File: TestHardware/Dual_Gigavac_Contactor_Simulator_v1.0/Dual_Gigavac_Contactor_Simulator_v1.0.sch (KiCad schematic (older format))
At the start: 69 parts, among them J1 Signal, J2 Power, J3 Contactor Driver 1, J4 Contactor Sense 2, J5 Contactor Sense 1, J6 Contactor Driver 2, Q1 Q_NMOS_DUAL_SGD, Q2 Q_NMOS_DUAL_SGD, Q3 Q_NMOS_DUAL_SGD, SW1 SW_Push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

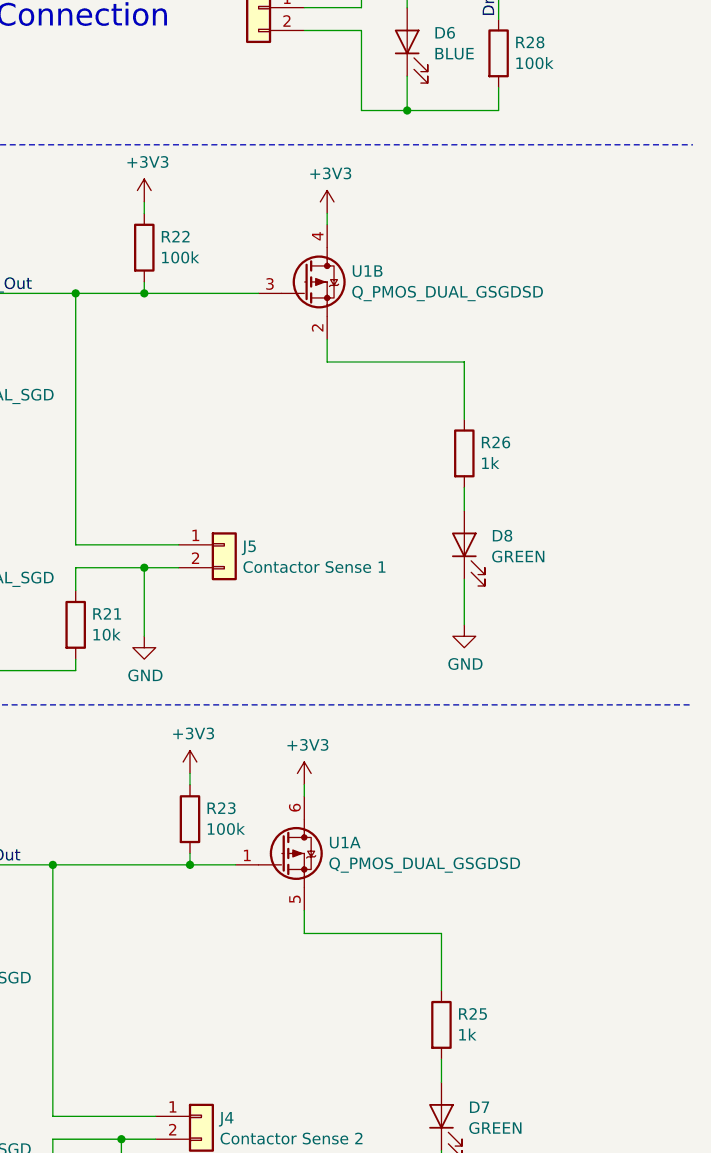
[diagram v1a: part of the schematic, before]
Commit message: Fix U1A & B Orientation
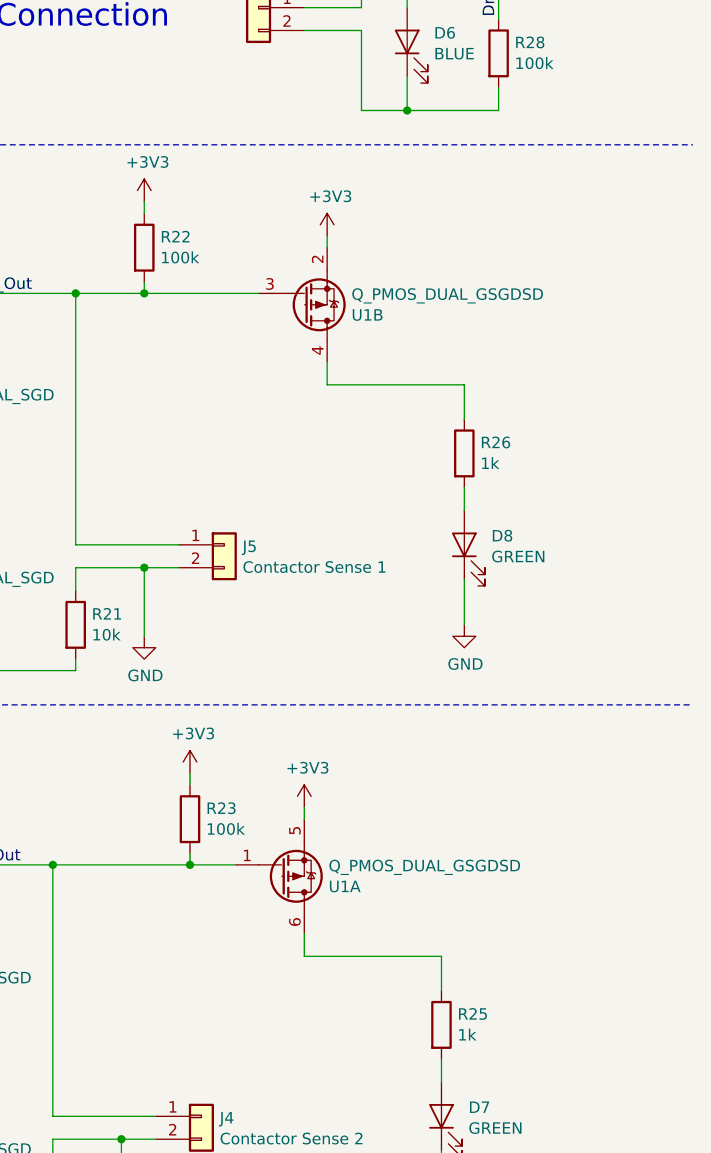
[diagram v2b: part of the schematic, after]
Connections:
- net +3V3: now also U1.2 (Source), U1.5 (Source); no longer U1.4 (Drain), U1.6 (Drain)
- net at R26.1: now also U1.4 (Drain); no longer U1.2 (Source)
- net at R25.1: now also U1.6 (Drain); no longer U1.5 (Source)
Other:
- moved on the sheet: U1A, U1B
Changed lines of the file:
@@
 EESchema Schematic File Version 4
+LIBS:Dual_Gigavac_Contactor_Simulator_v1.0-cache
 EELAYER 26 0
 EELAYER END
@@
 L Discrete_SMD:Q_PMOS_DUAL_GSGDSD U1
 U 2 1 5F0C1AAE
-P 8750 2450
-F 0 "U1" H 8906 2496 50  0000 L CNN
-F 1 "Q_PMOS_DUAL_GSGDSD" H 8906 2405 50  0000 L CNN
-F 2 "Package_TO_SOT_SMD:SuperSOT-6" H 8900 2550 50  0001 C CNN
-F 3 "https://www.onsemi.com/pub/Collateral/NDC7003P-D.PDF" H 8700 2450 50  0001 C CNN
-F 4 "NDC7003P " H 0   0   50  0001 C CNN "MPN"
-	2    8750 2450
-	1    0    0    -1
+P 8750 2550
+F 0 "U1" H 8906 2596 50  0000 L CNN
+F 1 "Q_PMOS_DUAL_GSGDSD" H 8906 2505 50  0000 L CNN
+F 2 "Package_TO_SOT_SMD:SuperSOT-6" H 8900 2650 50  0001 C CNN
+F 3 "https://www.onsemi.com/pub/Collateral/NDC7003P-D.PDF" H 8700 2550 50  0001 C CNN
+F 4 "NDC7003P " H 0   100 50  0001 C CNN "MPN"
+	2    8750 2550
+	1    0    0    1
 $EndComp
 $Comp
 L Discrete_SMD:Q_PMOS_DUAL_GSGDSD U1
 U 1 1 5F0C1B3D
-P 8650 4950
-F 0 "U1" H 8806 4996 50  0000 L CNN
-F 1 "Q_PMOS_DUAL_GSGDSD" H 8806 4905 50  0000 L CNN
-F 2 "Package_TO_SOT_SMD:SuperSOT-6" H 8800 5050 50  0001 C CNN
-F 3 "https://www.onsemi.com/pub/Collateral/NDC7003P-D.PDF" H 8600 4950 50  0001 C CNN
-F 4 "NDC7003P " H 0   0   50  0001 C CNN "MPN"
-	1    8650 4950
-	1    0    0    -1
+P 8650 5050
+F 0 "U1" H 8806 5096 50  0000 L CNN
+F 1 "Q_PMOS_DUAL_GSGDSD" H 8806 5005 50  0000 L CNN
+F 2 "Package_TO_SOT_SMD:SuperSOT-6" H 8800 5150 50  0001 C CNN
+F 3 "https://www.onsemi.com/pub/Collateral/NDC7003P-D.PDF" H 8600 5050 50  0001 C CNN
+F 4 "NDC7003P " H 0   100 50  0001 C CNN "MPN"
+	1    8650 5050
+	1    0    0    1
 $EndComp
 Wire Wire Line
@@
 L power:+3V3 #PWR011
 U 1 1 5F124D0E
-P 8800 2150
-F 0 "#PWR011" H 8800 2000 50  0001 C CNN
-F 1 "+3V3" H 8815 2323 50  0000 C CNN
-F 2 "" H 8800 2150 50  0001 C CNN
-F 3 "" H 8800 2150 50  0001 C CNN
-	1    8800 2150
-	1    0    0    -1
-$EndComp
-Wire Wire Line
-	8800 2200 8800 2150
+P 8800 2250
+F 0 "#PWR011" H 8800 2100 50  0001 C CNN
+F 1 "+3V3" H 8815 2423 50  0000 C CNN
+F 2 "" H 8800 2250 50  0001 C CNN
+F 3 "" H 8800 2250 50  0001 C CNN
+	1    8800 2250
+	1    0    0    -1
+$EndComp
+Wire Wire Line
+	8800 2300 8800 2250
 $Comp
 L power:+3V3 #PWR010
 U 1 1 5F12A931
-P 8700 4650
-F 0 "#PWR010" H 8700 4500 50  0001 C CNN
-F 1 "+3V3" H 8715 4823 50  0000 C CNN
-F 2 "" H 8700 4650 50  0001 C CNN
-F 3 "" H 8700 4650 50  0001 C CNN
-	1    8700 4650
-	1    0    0    -1
-$EndComp
-Wire Wire Line
-	8700 4700 8700 4650
+P 8700 4750
+F 0 "#PWR010" H 8700 4600 50  0001 C CNN
+F 1 "+3V3" H 8715 4923 50  0000 C CNN
+F 2 "" H 8700 4750 50  0001 C CNN
+F 3 "" H 8700 4750 50  0001 C CNN
+	1    8700 4750
+	1    0    0    -1
+$EndComp
+Wire Wire Line
+	8700 4800 8700 4750
 $Comp
 L device:R R26
@@
 	9400 3450 9400 3350
 Wire Wire Line
-	9400 3050 9400 2800
-Wire Wire Line
-	9400 2800 8800 2800
-Wire Wire Line
-	8800 2800 8800 2700
+	9400 3050 9400 2900
+Wire Wire Line
+	8800 2900 8800 2800
 $Comp
 L power:GND #PWR013
@@
 	9300 5950 9300 5850
 Wire Wire Line
-	9300 5550 9300 5300
-Wire Wire Line
-	9300 5300 8700 5300
+	9300 5550 9300 5400
 $Comp
 L power:GND #PWR012
@@
 	9300 6450 9300 6250
 Wire Wire Line
-	8700 5300 8700 5200
+	8700 5400 8700 5300
 Wire Notes Line
 	3700 550  3700 7850
@@
 Wire Wire Line
 	5400 4950 5400 5000
+Wire Wire Line
+	8800 2900 9400 2900
+Wire Wire Line
+	8700 5400 9300 5400
 $EndSCHEMATC

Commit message: Updates from other repo
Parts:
- removed Q1, Q2, Q3: Q_NMOS_DUAL_SGD, Package_TO_SOT_SMD:SOT-363_SC-70-6, symbol Discrete_SMD:Q_NMOS_DUAL_SGD
- added C2, C3, C4, C5, C6, C7, C8, C9: 0.1uF, Capacitor_SMD:C_0603_1608Metric_Pad1.05x0.95mm_HandSolder, symbol device:C
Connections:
- net Driver_1: now also C6.1
- net Driver_2: now also C9.1
- net EN_1: now also C3.1
- net EN_2: now also C5.1
- net GND: now also C2.2, C3.2, C4.2, C5.2, C7.2, C8.2
- net Sense1_Out: now also C8.1
- net Sense2_Out: now also C7.1
- net WELD_1: now also C2.1
- net WELD_2: now also C4.1
- net Sense1_Pull: now reaches R21.2
- net at D6.1 (K), J6.2 (Pin_2), R28.2: now also C9.2
- net Sense2_Pull: now reaches R20.2
- net at D5.1 (K), J3.2 (Pin_2), R19.2: now also C6.2
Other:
- note added: "Logic for Normally Closed\nAuxillary Contacts"
- note added: "Logic for Normally Open\nAuxillary Contacts"
- note added: "Output Logic\nPopulate One"
- note added: "Truth Table for Sense Output\n+--------+----+---+----+----+\n|Enable/Weld | 00 | 01 | 11 | 10 |\n+--------+----+---+----+----+\n| Driver OFF | N | W | W | N | \n| Driver ON | F | N | N | N | \n+--------+----+---+----+----+\nN = Normal Operation\nW = Weld\nF = Failed Contactor\n\nSee Sheets of NC/NO Logic for specific truth tables\n"
- note removed: "Truth Table for Sense Output\n+--------+----+---+----+----+\n|Enable/Weld | 00 | 01 | 11 | 10 |\n+--------+----+---+----+----+\n| Driver OFF | 0 | 1! | 1! | 0 | \n| Driver ON | 0* | 1 | 1 | 1 | \n+--------+----+---+----+----+\n* Should detect issue with contactor\n! Should detect welded contactor"
- moved on the sheet: D6, D7, D8, J4, J5, J6, R10, R12, R13, R15, R20, R21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
